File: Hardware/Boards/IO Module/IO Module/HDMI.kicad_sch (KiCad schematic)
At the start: 61 parts, among them J4 HDMI_A, U10 TPD4E02B04DQA, U19 TPS74801AWDRC, U20 PCA9517ATP, U21 TXB0108DQSR, U25 TPD4E02B04DQA, U27 L78L05_SOT89, U5 SN75DP159RSB, U7 TPD5S116

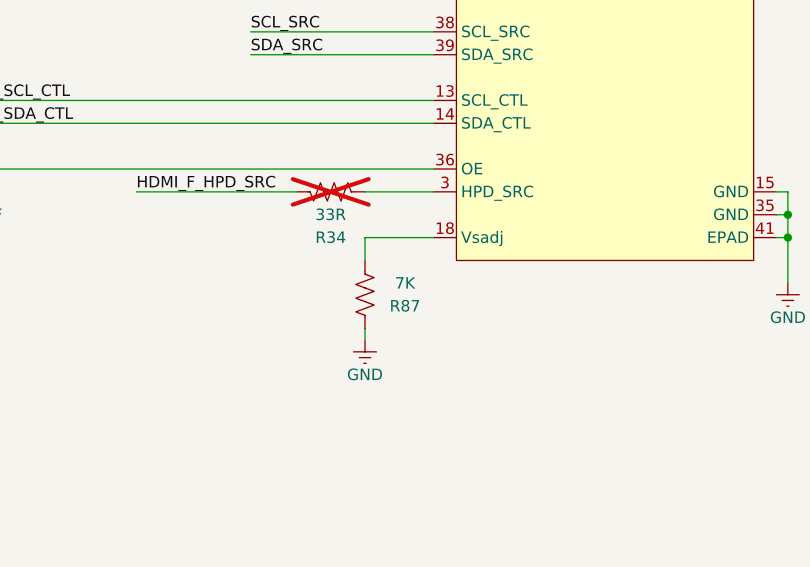
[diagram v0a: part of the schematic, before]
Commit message: Updated SCH and Layout
Added temp sensors for DCDC's, Added MCU control for FPGA mode, removed mode DIP switch
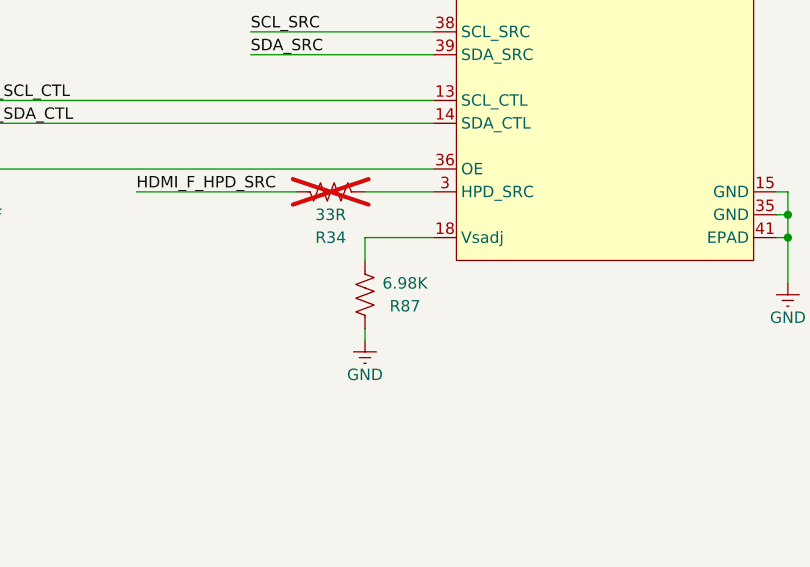
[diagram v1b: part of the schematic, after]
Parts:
- R87: value 7K -> 6.98K
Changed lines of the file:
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@@
 			)
 		)
-		(property "Value" "7K"
+		(property "Value" "6.98K"
 			(at 202.565 161.29 0)
 			(effects
